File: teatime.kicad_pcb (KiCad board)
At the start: 2 copper layers, 100 x 100 mm, 64 parts, among them Q1 NCV8402, Q2 NCV8402, Q3 NCV8402, Q4 NCV8402, Q5 NCV8402, Q6 NCV8402, Q7 NCV8402, Q8 NCV8402, SW1 SW_Push, U1 NCP1117-3.3_SOT223, U2 74HC4051

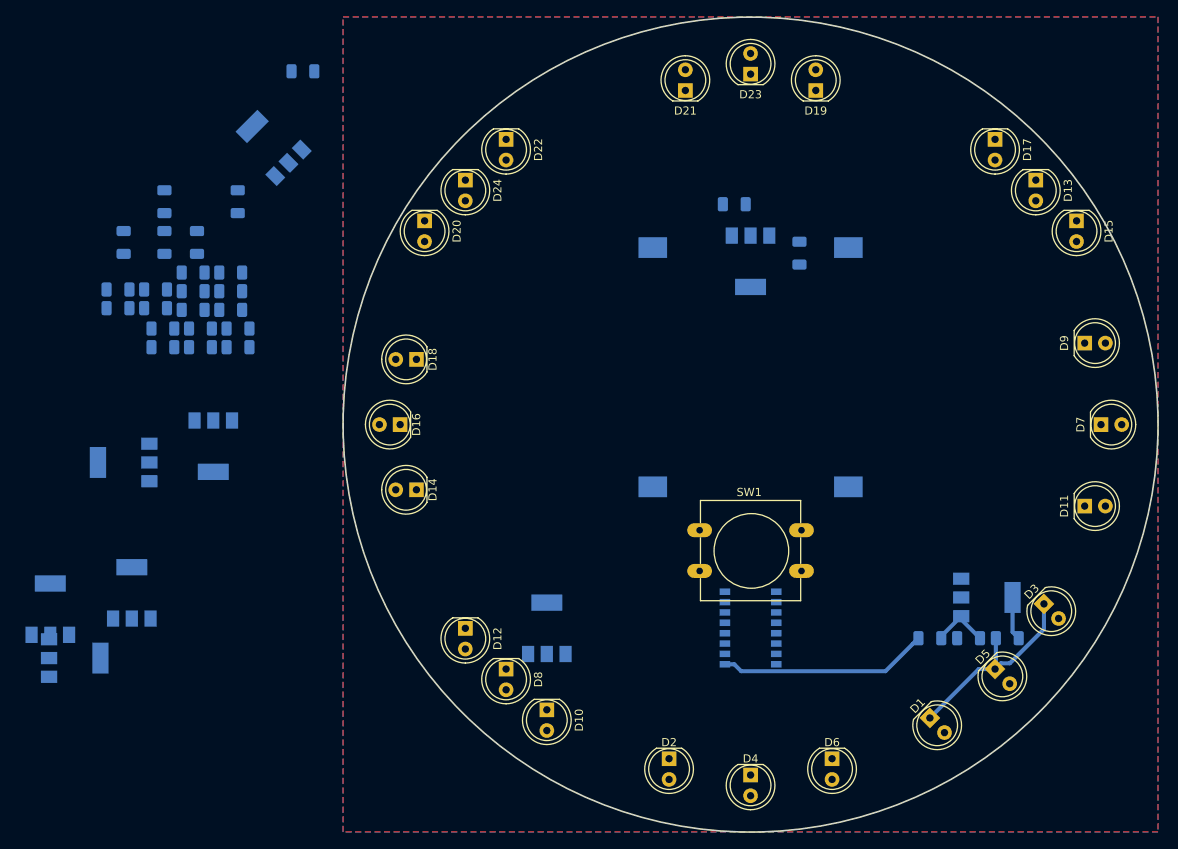
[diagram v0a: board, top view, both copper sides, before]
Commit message: Shift regs and led layout
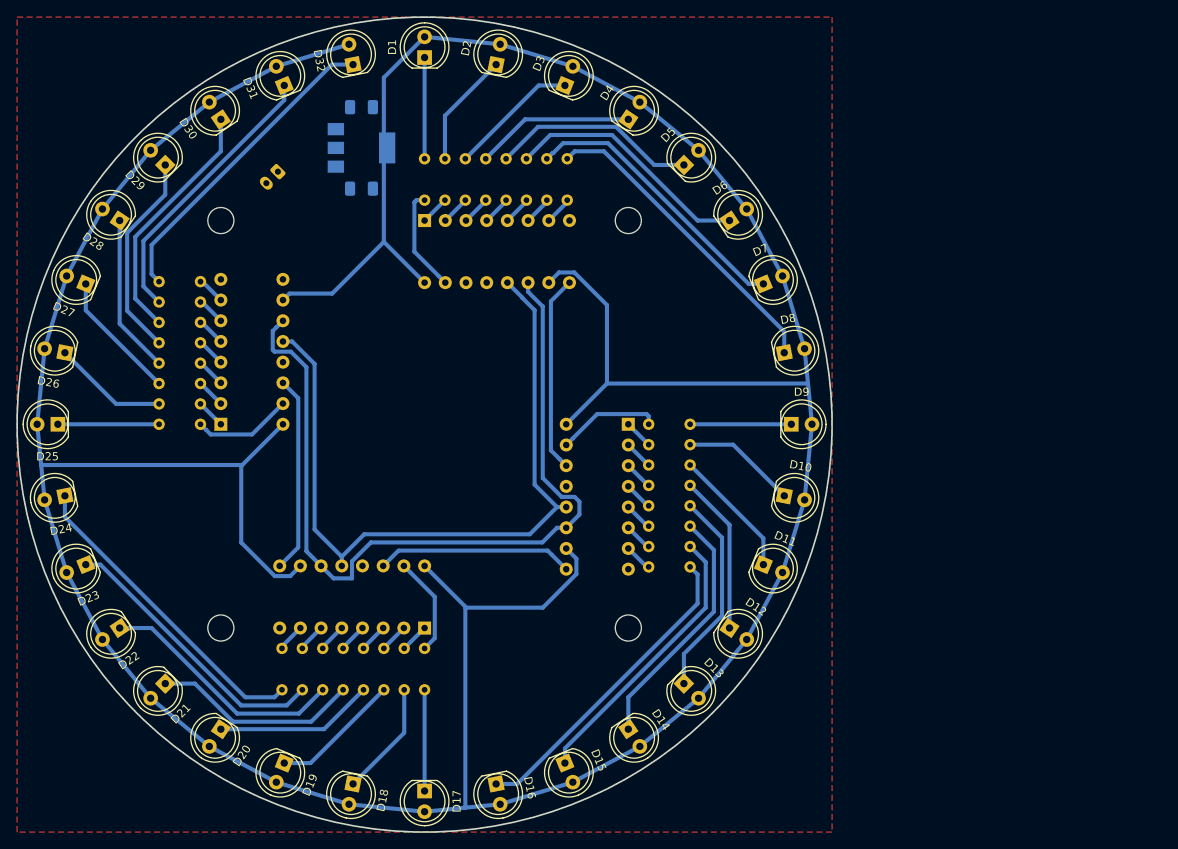
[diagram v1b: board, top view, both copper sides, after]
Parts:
- removed BT2: Battery_Cell, Battery:BatteryHolder_Keystone_1058_1x2032
- removed Q1, Q2, Q3, Q4, Q5, Q6, Q7, Q8: NCV8402, Package_TO_SOT_SMD:SOT-223-3_TabPin2
- removed SW1: SW_Push, Button_Switch_THT:SW_PUSH-12mm
- added D25: LED, LED_THT:LED_D5.0mm, F.Cu at (55.0, 100.0)
- added D26: LED, LED_THT:LED_D5.0mm, F.Cu at (55.9, 91.2)
- added D27: LED, LED_THT:LED_D5.0mm, F.Cu at (58.4, 82.8)
- added D28: LED, LED_THT:LED_D5.0mm, F.Cu at (62.6, 75.0)
- added D29: LED, LED_THT:LED_D5.0mm, F.Cu at (68.2, 68.2)
- added D30: LED, LED_THT:LED_D5.0mm, F.Cu at (75.0, 62.6)
- added D31: LED, LED_THT:LED_D5.0mm, F.Cu at (82.8, 58.4)
- added D32: LED, LED_THT:LED_D5.0mm, F.Cu at (91.2, 55.9)
- added H1: MountingHole, MountingHole:MountingHole_3.2mm_M3, F.Cu at (75.0, 75.0)
- added H2: MountingHole, MountingHole:MountingHole_3.2mm_M3, F.Cu at (125.0, 75.0)
- added H3: MountingHole, MountingHole:MountingHole_3.2mm_M3, F.Cu at (125.0, 125.0)
- added H4: MountingHole, MountingHole:MountingHole_3.2mm_M3, F.Cu at (75.0, 125.0)
- added R26: 680r, Resistor_THT:R_Axial_DIN0204_L3.6mm_D1.6mm_P5.08mm_Horizontal, B.Cu at (72.5, 97.5)
- added R27: 680r, Resistor_THT:R_Axial_DIN0204_L3.6mm_D1.6mm_P5.08mm_Horizontal, B.Cu at (72.5, 95.0)
- added R28: 680r, Resistor_THT:R_Axial_DIN0204_L3.6mm_D1.6mm_P5.08mm_Horizontal, B.Cu at (72.5, 92.5)
- added R29: 680r, Resistor_THT:R_Axial_DIN0204_L3.6mm_D1.6mm_P5.08mm_Horizontal, B.Cu at (72.5, 90.0)
- added R30: 680r, Resistor_THT:R_Axial_DIN0204_L3.6mm_D1.6mm_P5.08mm_Horizontal, B.Cu at (72.5, 87.5)
- added R31: 680r, Resistor_THT:R_Axial_DIN0204_L3.6mm_D1.6mm_P5.08mm_Horizontal, B.Cu at (72.5, 85.0)
- added R32: 680r, Resistor_THT:R_Axial_DIN0204_L3.6mm_D1.6mm_P5.08mm_Horizontal, B.Cu at (72.5, 82.5)
- added U3: 74HC596, Package_DIP:DIP-16_W7.62mm, B.Cu at (125.0, 100.0)
- added U4: 74HC596, Package_DIP:DIP-16_W7.62mm, B.Cu at (100.0, 125.0)
- added U5: 74HC596, Package_DIP:DIP-16_W7.62mm, B.Cu at (75.0, 100.0)
- BT1: footprint Battery:BatteryHolder_Keystone_1058_1x2032 -> Connector_JST:JST_PH_S2B-PH-K_1x02_P2.00mm_Horizontal
- D1, D10, D11, D12, D13, D14, D15, D16, D17, D18, D19, D2, D20, D21, D22, D23, D24, D3, D4, D5, D6, D7, D8, D9: footprint LED_THT:LED_D5.0mm_Clear -> LED_THT:LED_D5.0mm
- R1, R12, R13, R18, R19, R2, R24, R25, R7: value R_Small -> 680r; footprint Resistor_SMD:R_1206_3216Metric -> Resistor_THT:R_Axial_DIN0204_L3.6mm_D1.6mm_P5.08mm_Horizontal
- R10, R11, R16, R17, R22, R23, R5, R6: value 100k -> 680r; footprint Resistor_SMD:R_1206_3216Metric -> Resistor_THT:R_Axial_DIN0204_L3.6mm_D1.6mm_P5.08mm_Horizontal
- R14, R15, R20, R21, R3, R4, R8, R9: value 1k -> 680r; footprint Resistor_SMD:R_1206_3216Metric -> Resistor_THT:R_Axial_DIN0204_L3.6mm_D1.6mm_P5.08mm_Horizontal
- U2: value 74HC4051 -> 74HC596; footprint Package_SO:SOP-16_4.4x10.4mm_P1.27mm -> Package_DIP:DIP-16_W7.62mm
- moved D17 106.3 mm to (100.0, 145.0)
- moved D19 105.2 mm to (82.8, 141.6), turned to 247.5 degrees
- moved D1 102.0 mm to (100.0, 55.0), turned to 90 degrees
- moved D23 101.4 mm to (58.4, 117.2), turned to 202.5 degrees
- moved D21 96.8 mm to (68.2, 131.8), turned to 225 degrees
- moved D15 91.5 mm to (117.2, 141.6), turned to 292.5 degrees
- moved D2 87.8 mm to (108.8, 55.9), turned to 78.75 degrees
- moved R2 87.5 mm to (102.5, 72.5), turned to 90 degrees
- moved D3 86.6 mm to (117.2, 58.4), turned to 67.5 degrees
- moved D4 81.8 mm to (125.0, 62.6), turned to 56.25 degrees
- moved R3 78.3 mm to (105.0, 72.5), turned to 90 degrees
- moved R5 78.2 mm to (110.0, 72.5), turned to 90 degrees
- moved D22 76.4 mm to (62.6, 125.0), turned to 213.75 degrees
- moved D13 75.4 mm to (131.8, 131.8), turned to 315 degrees
- moved BT1 74.0 mm to (82.0, 69.0), turned to 225 degrees
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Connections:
- BT1 pad 2: Net-(BT1-Pad2) -> GND
- C2 pad 1: VCC -> +3V3
- D1 pad 2: VCC -> +3V3
- D10 pad 2: VCC -> +3V3
- D11 pad 2: VCC -> +3V3
- D12 pad 1: Net-(D10-Pad1) -> Net-(D12-Pad1)
- D12 pad 2: VCC -> +3V3
- D13 pad 2: VCC -> +3V3
- D14 pad 2: VCC -> +3V3
- D15 pad 1: Net-(D13-Pad1) -> Net-(D15-Pad1)
- D15 pad 2: VCC -> +3V3
- D16 pad 1: Net-(D14-Pad1) -> Net-(D16-Pad1)
- D16 pad 2: VCC -> +3V3
- D17 pad 1: Net-(D13-Pad1) -> Net-(D17-Pad1)
- D17 pad 2: VCC -> +3V3
- D18 pad 1: Net-(D14-Pad1) -> Net-(D18-Pad1)
- D18 pad 2: VCC -> +3V3
- D19 pad 2: VCC -> +3V3
- D2 pad 2: VCC -> +3V3
- D20 pad 2: VCC -> +3V3
- D21 pad 1: Net-(D19-Pad1) -> Net-(D21-Pad1)
- D21 pad 2: VCC -> +3V3
- D22 pad 1: Net-(D20-Pad1) -> Net-(D22-Pad1)
- D22 pad 2: VCC -> +3V3
- D23 pad 1: Net-(D19-Pad1) -> Net-(D23-Pad1)
- D23 pad 2: VCC -> +3V3
- D24 pad 1: Net-(D20-Pad1) -> Net-(D24-Pad1)
- D24 pad 2: VCC -> +3V3
- D3 pad 1: Net-(D1-Pad1) -> Net-(D3-Pad1)
- D3 pad 2: VCC -> +3V3
- D4 pad 1: Net-(D2-Pad1) -> Net-(D4-Pad1)
- D4 pad 2: VCC -> +3V3
- D5 pad 1: Net-(D1-Pad1) -> Net-(D5-Pad1)
- D5 pad 2: VCC -> +3V3
- D6 pad 1: Net-(D2-Pad1) -> Net-(D6-Pad1)
- D6 pad 2: VCC -> +3V3
- D7 pad 1: Net-(D11-Pad1) -> Net-(D7-Pad1)
- D7 pad 2: VCC -> +3V3
- D8 pad 1: Net-(D10-Pad1) -> Net-(D8-Pad1)
- D8 pad 2: VCC -> +3V3
- D9 pad 1: Net-(D11-Pad1) -> Net-(D9-Pad1)
- D9 pad 2: VCC -> +3V3
- R1 pad 2: GND -> Net-(D1-Pad1)
- R10 pad 1: Net-(Q3-Pad1) -> Net-(R10-Pad1)
- R10 pad 2: GND -> Net-(D10-Pad1)
- R11 pad 1: Net-(Q4-Pad1) -> Net-(R11-Pad1)
- R11 pad 2: GND -> Net-(D11-Pad1)
- R12 pad 1: Net-(D11-Pad1) -> Net-(R12-Pad1)
- R12 pad 2: Net-(Q3-Pad2) -> Net-(D12-Pad1)
- R13 pad 1: Net-(D10-Pad1) -> Net-(R13-Pad1)
- R13 pad 2: Net-(Q4-Pad2) -> Net-(D13-Pad1)
- R14 pad 1: Net-(Q5-Pad1) -> Net-(R14-Pad1)
- R14 pad 2: Net-(R14-Pad2) -> Net-(D14-Pad1)
- R15 pad 1: Net-(Q6-Pad1) -> Net-(R15-Pad1)
- R15 pad 2: Net-(R15-Pad2) -> Net-(D15-Pad1)
- R16 pad 1: Net-(Q5-Pad1) -> Net-(R16-Pad1)
- R16 pad 2: GND -> Net-(D16-Pad1)
- R17 pad 1: Net-(Q6-Pad1) -> Net-(R17-Pad1)
- R17 pad 2: GND -> Net-(D17-Pad1)
- R18 pad 1: Net-(D13-Pad1) -> Net-(R18-Pad1)
- R18 pad 2: Net-(Q5-Pad2) -> Net-(D18-Pad1)
- R19 pad 1: Net-(D14-Pad1) -> Net-(R19-Pad1)
- R19 pad 2: Net-(Q6-Pad2) -> Net-(D19-Pad1)
- R2 pad 1: Net-(D1-Pad1) -> Net-(R2-Pad1)
- R2 pad 2: Net-(Q1-Pad2) -> Net-(D2-Pad1)
- R20 pad 1: Net-(Q7-Pad1) -> Net-(R20-Pad1)
- R20 pad 2: Net-(R20-Pad2) -> Net-(D20-Pad1)
- R21 pad 1: Net-(Q8-Pad1) -> Net-(R21-Pad1)
- R21 pad 2: Net-(R21-Pad2) -> Net-(D21-Pad1)
- R22 pad 1: Net-(Q7-Pad1) -> Net-(R22-Pad1)
- R22 pad 2: GND -> Net-(D22-Pad1)
- R23 pad 1: Net-(Q8-Pad1) -> Net-(R23-Pad1)
- R23 pad 2: GND -> Net-(D23-Pad1)
- R24 pad 1: Net-(D19-Pad1) -> Net-(R24-Pad1)
- R24 pad 2: Net-(Q7-Pad2) -> Net-(D24-Pad1)
- R25 pad 1: Net-(D20-Pad1) -> Net-(R25-Pad1)
- R3 pad 1: Net-(Q1-Pad1) -> Net-(R3-Pad1)
- R3 pad 2: Net-(R3-Pad2) -> Net-(D3-Pad1)
- R4 pad 1: Net-(Q2-Pad1) -> Net-(R4-Pad1)
- R4 pad 2: Net-(R4-Pad2) -> Net-(D4-Pad1)
- R5 pad 1: Net-(Q1-Pad1) -> Net-(R5-Pad1)
- R5 pad 2: GND -> Net-(D5-Pad1)
- R6 pad 1: Net-(Q2-Pad1) -> Net-(R6-Pad1)
- R6 pad 2: GND -> Net-(D6-Pad1)
- R7 pad 1: Net-(D2-Pad1) -> Net-(R7-Pad1)
- R7 pad 2: Net-(Q2-Pad2) -> Net-(D7-Pad1)
- R8 pad 1: Net-(Q3-Pad1) -> Net-(R8-Pad1)
- R8 pad 2: Net-(R8-Pad2) -> Net-(D8-Pad1)
- R9 pad 1: Net-(Q4-Pad1) -> Net-(R9-Pad1)
- R9 pad 2: Net-(R9-Pad2) -> Net-(D9-Pad1)
- U1 pad 2: VCC -> +3V3
- U2 pad 1: Net-(R3-Pad2) -> Net-(R2-Pad1)
- U2 pad 10: Net-(U2-Pad10) -> +3V3
- U2 pad 12: Net-(R21-Pad2) -> Net-(U2-Pad12)
- U2 pad 13: Net-(R14-Pad2) -> GND
- U2 pad 14: Net-(R20-Pad2) -> Net-(U2-Pad14)
- U2 pad 15: Net-(R15-Pad2) -> Net-(R1-Pad1)
- U2 pad 16: VCC -> +3V3
- U2 pad 2: Net-(R4-Pad2) -> Net-(R3-Pad1)
- U2 pad 3: Net-(U2-Pad3) -> Net-(R4-Pad1)
- U2 pad 4: Net-(R9-Pad2) -> Net-(R5-Pad1)
- U2 pad 5: Net-(R8-Pad2) -> Net-(R6-Pad1)
- U2 pad 6: GND -> Net-(R7-Pad1)
- U2 pad 7: GND -> Net-(R8-Pad1)
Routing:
- net +3V3: track 0.00 -> 490.7 mm
- net Net-(U2-Pad11): track 0.00 -> 103.0 mm
- net Net-(U2-Pad12): track 0.00 -> 91.3 mm
- net Net-(D24-Pad1): track 0.00 -> 38.8 mm
- net Net-(D16-Pad1): track 0.00 -> 38.8 mm
- net Net-(D32-Pad1): track 0.00 -> 38.8 mm
- net Net-(D8-Pad1): track 0.00 -> 38.8 mm
- net Net-(D23-Pad1): track 0.00 -> 34.5 mm
- net Net-(D31-Pad1): track 0.00 -> 34.5 mm
- net Net-(D15-Pad1): track 0.00 -> 34.5 mm
- net Net-(D7-Pad1): track 0.00 -> 34.5 mm
- net Net-(D22-Pad1): track 0.00 -> 30.5 mm
- net Net-(D30-Pad1): track 0.00 -> 30.5 mm
- net Net-(D14-Pad1): track 0.00 -> 30.5 mm
- net Net-(D6-Pad1): track 0.00 -> 30.5 mm
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- added copper zone on F.Cu, net GND
- removed copper zone on B.Cu, net GND
- removed copper zone on F.Cu, net VCC
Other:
- net class Default: trace_width 0.25 -> 0.5; via_dia 0.8 -> 0.6; via_drill 0.4 -> 0.3

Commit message: Add micro and tweak some other bits
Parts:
- added R33: 100k, Resistor_THT:R_Axial_DIN0204_L3.6mm_D1.6mm_P5.08mm_Horizontal, F.Cu at (107.5, 97.5)
- added SW1: SW_Push, Button_Switch_THT:SW_PUSH_6mm, F.Cu at (97.5, 97.5)
- added U6: ATtiny85-20PU, Package_DIP:DIP-8_W7.62mm, F.Cu at (97.5, 95.0)
- R1, R10, R11, R12, R13, R14, R15, R16, R17, R18, R19, R2, R20, R21, R22, R23, R24, R25, R26, R27, R28, R29, R3, R30, R31, R32, R4, R5, R6, R7, R8, R9: value 680r -> 220r; moved to F.Cu
- U1: value NCP1117-3.3_SOT223 -> MCP1700-3302E_TO92; footprint Package_TO_SOT_SMD:SOT-223-3_TabPin2 -> Package_TO_SOT_THT:TO-92_Inline; moved to F.Cu
- U2, U3, U4, U5: moved to F.Cu
- moved R32 113.0 mm to (184.6, 97.0), turned to 0 degrees
- moved R25 112.5 mm to (184.6, 90.7), turned to 0 degrees
- moved R31 112.5 mm to (184.6, 93.8), turned to 0 degrees
- moved R30 105.3 mm to (176.6, 103.2), turned to 0 degrees
- moved R22 105.0 mm to (184.6, 87.5), turned to 0 degrees
- moved R29 104.6 mm to (176.6, 100.1), turned to 0 degrees
- moved R26 104.1 mm to (176.6, 97.0), turned to 0 degrees
- moved R24 99.9 mm to (176.6, 93.8), turned to 0 degrees
- moved R28 97.1 mm to (168.6, 106.4), turned to 0 degrees
- moved R27 96.4 mm to (168.6, 103.2), turned to 0 degrees
- moved R23 87.9 mm to (168.6, 100.1), turned to 0 degrees
- moved R18 87.3 mm to (176.6, 90.7), turned to 0 degrees
- moved R19 79.7 mm to (168.6, 97.0), turned to 0 degrees
- moved R17 76.4 mm to (168.6, 93.8), turned to 0 degrees
- moved R21 73.6 mm to (160.5, 106.4), turned to 0 degrees
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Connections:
- U1 pad 2: +3V3 -> Net-(BT1-Pad1)
- U1 pad 3: Net-(BT1-Pad1) -> +3V3
- U5 pad 9: Net-(U5-Pad9) -> (no net)
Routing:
- net +3V3: track 490.7 -> 0.00 mm
- net Net-(U2-Pad11): track 103.0 -> 0.00 mm
- net Net-(U2-Pad12): track 91.3 -> 0.00 mm
- net Net-(D24-Pad1): track 38.8 -> 0.00 mm
- net Net-(D16-Pad1): track 38.8 -> 0.00 mm
- net Net-(D32-Pad1): track 38.8 -> 0.00 mm
- net Net-(D8-Pad1): track 38.8 -> 0.00 mm
- net Net-(D23-Pad1): track 34.5 -> 0.00 mm
- net Net-(D31-Pad1): track 34.5 -> 0.00 mm
- net Net-(D15-Pad1): track 34.5 -> 0.00 mm
- net Net-(D7-Pad1): track 34.5 -> 0.00 mm
- net Net-(D22-Pad1): track 30.5 -> 0.00 mm
- net Net-(D30-Pad1): track 30.5 -> 0.00 mm
- net Net-(D14-Pad1): track 30.5 -> 0.00 mm
- net Net-(D6-Pad1): track 30.5 -> 0.00 mm
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
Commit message: More tweaks and v1 version of board
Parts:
- added C3: 100n, Capacitor_THT:C_Disc_D3.0mm_W1.6mm_P2.50mm, F.Cu at (106.5, 90.0)
- C1, C2: value 10u -> 1u; moved to F.Cu
- moved R15 107.7 mm to (72.5, 115.0), turned to 180 degrees
- moved R11 97.1 mm to (72.5, 105.0), turned to 180 degrees
- moved D25 90.0 mm to (145.0, 100.0), turned to 0 degrees
- moved D9 90.0 mm to (55.0, 100.0), turned to 180 degrees
- moved R16 89.7 mm to (72.5, 117.5), turned to 180 degrees
- moved R12 88.7 mm to (72.5, 107.5), turned to 180 degrees
- moved R10 88.5 mm to (72.5, 102.5), turned to 180 degrees
- moved D10 88.3 mm to (55.9, 108.8), turned to 191.25 degrees
- moved D24 88.3 mm to (144.1, 108.8), turned to 348.75 degrees
- moved D26 88.3 mm to (144.1, 91.2), turned to 11.25 degrees
- moved D8 88.3 mm to (55.9, 91.2), turned to 168.75 degrees
- moved R8 87.4 mm to (82.5, 72.5), turned to 90 degrees
- moved D11 83.1 mm to (58.4, 117.2), turned to 202.5 degrees
- moved D23 83.1 mm to (141.6, 117.2), turned to 337.5 degrees
- moved D27 83.1 mm to (141.6, 82.8), turned to 22.5 degrees
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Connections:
- U5 pad 9: (no net) -> Net-(U5-Pad9)
- U6 pad 2: (no net) -> Net-(U6-Pad2)
- U6 pad 3: (no net) -> Net-(U6-Pad3)
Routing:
- net +3V3: track 0.00 -> 517.4 mm
- net Net-(U2-Pad11): track 0.00 -> 120.1 mm
- net Net-(U2-Pad12): track 0.00 -> 102.2 mm
- net Net-(D8-Pad1): track 0.00 -> 38.8 mm
- net Net-(D32-Pad1): track 0.00 -> 38.8 mm
- net Net-(D16-Pad1): track 0.00 -> 38.8 mm
- net Net-(D24-Pad1): track 0.00 -> 38.8 mm
- net Net-(D7-Pad1): track 0.00 -> 34.5 mm
- net Net-(D15-Pad1): track 0.00 -> 34.5 mm
- net Net-(D31-Pad1): track 0.00 -> 34.5 mm
- net Net-(D23-Pad1): track 0.00 -> 34.5 mm
- net Net-(D14-Pad1): track 0.00 -> 30.5 mm
- net Net-(D6-Pad1): track 0.00 -> 30.5 mm
- net Net-(D22-Pad1): track 0.00 -> 30.5 mm
- net Net-(D30-Pad1): track 0.00 -> 30.5 mm
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- added copper zone on B.Cu, net GND
- removed copper zone on F.Cu, net GND
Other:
- net class vcc added: clearance 0.2, trace_width 1, via_dia 0.6, via_drill 0.3

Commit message: Few slight tweaks to footprints used and updated build files
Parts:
- C3: footprint Capacitor_THT:C_Disc_D3.0mm_W1.6mm_P2.50mm -> Capacitor_SMD:C_1206_3216Metric
- U1: footprint Package_TO_SOT_THT:TO-92_Inline -> Package_TO_SOT_THT:TO-92_Inline_W4.0mm_Horizontal_FlatSideDown
- U2, U3, U4, U5: value 74HC596 -> 74HC595
- moved C3 1.25 mm to (106.5, 91.2)
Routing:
- net GND: track 13.5 -> 17.8 mm

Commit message: Few small tweaks and add silk
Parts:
- added C4: 100n, Capacitor_SMD:C_1206_3216Metric, F.Cu at (103.8, 81.2)
- added C5: 100n, Capacitor_SMD:C_1206_3216Metric, F.Cu at (81.0, 96.2)
- added C6: 100n, Capacitor_SMD:C_1206_3216Metric, F.Cu at (96.2, 119.0)
- added C7: 100n, Capacitor_SMD:C_1206_3216Metric, F.Cu at (119.0, 103.8)
- added HS1: QR, teatime:__github.com_HarkonenBade_teatime, B.Cu at (70.0, 87.5)
- R1, R10, R11, R12, R13, R14, R15, R16, R17, R18, R19, R2, R20, R21, R22, R23, R24, R25, R26, R27, R28, R29, R3, R30, R31, R32, R33, R4, R5, R6, R7, R8, R9: footprint Resistor_THT:R_Axial_DIN0204_L3.6mm_D1.6mm_P5.08mm_Horizontal -> Resistor_THT:R_Axial_DIN0204_L3.6mm_D1.6mm_P7.62mm_Horizontal
- U1: value MCP1700-3302E_TO92 -> MCP1700-3302E
- moved R33 2.12 mm to (93.0, 95.0)
- moved R16 0.28 mm to (72.5, 117.8)
- moved R24 0.28 mm to (117.8, 127.5)
- moved R32 0.28 mm to (127.5, 82.2)
- moved R8 0.28 mm to (82.2, 72.5)
- moved R15 0.24 mm to (72.5, 115.2)
- moved R23 0.24 mm to (115.2, 127.5)
- moved R31 0.24 mm to (127.5, 84.8)
- moved R7 0.24 mm to (84.8, 72.5)
- moved R14 0.20 mm to (72.5, 112.7)
- moved R22 0.20 mm to (112.7, 127.5)
- moved R30 0.20 mm to (127.5, 87.3)
- moved R6 0.20 mm to (87.3, 72.5)
- moved R13 0.16 mm to (72.5, 110.2)
- moved R21 0.16 mm to (110.2, 127.5)
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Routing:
- net GND: track 17.8 -> 22.2 mm, vias 0 -> 4
- net Net-(D2-Pad1): track 14.2 -> 11.6 mm
- net Net-(D10-Pad1): track 14.2 -> 11.6 mm
- net Net-(D26-Pad1): track 14.2 -> 11.6 mm
- net Net-(D18-Pad1): track 14.2 -> 11.6 mm
- net Net-(D9-Pad1): track 12.4 -> 9.88 mm
- net Net-(D1-Pad1): track 12.4 -> 9.88 mm
- net Net-(D25-Pad1): track 12.4 -> 9.88 mm
- net Net-(D17-Pad1): track 12.4 -> 9.88 mm
- net Net-(R33-Pad1): track 14.7 -> 12.6 mm
- net +3V3: track 517.4 -> 515.4 mm
- net Net-(D20-Pad1): track 19.5 -> 20.1 mm
- net Net-(D4-Pad1): track 19.5 -> 20.1 mm
- net Net-(D28-Pad1): track 19.5 -> 20.1 mm
- net Net-(D12-Pad1): track 19.5 -> 20.1 mm
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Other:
- board text added: "+"
- board text added: "-"
- board text added: "Lithium Primary 3.5V Min"
- board text added: "Teatime HarkonenBade 2020-02-14 Rev 1"
- board text added: "https://github.com/HarkonenBade/teatime"

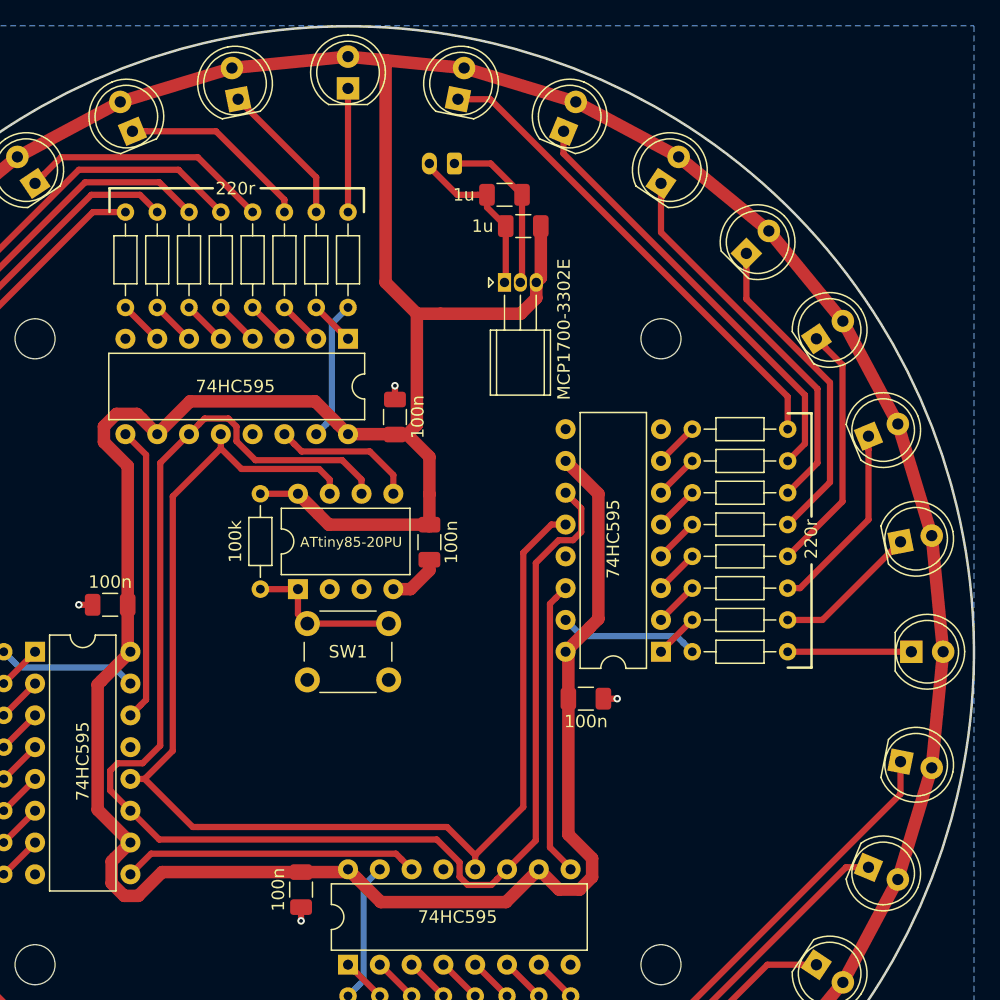
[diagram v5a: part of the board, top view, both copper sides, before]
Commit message: Switch around various bits: * Add decoupling * Omron button * pth caps
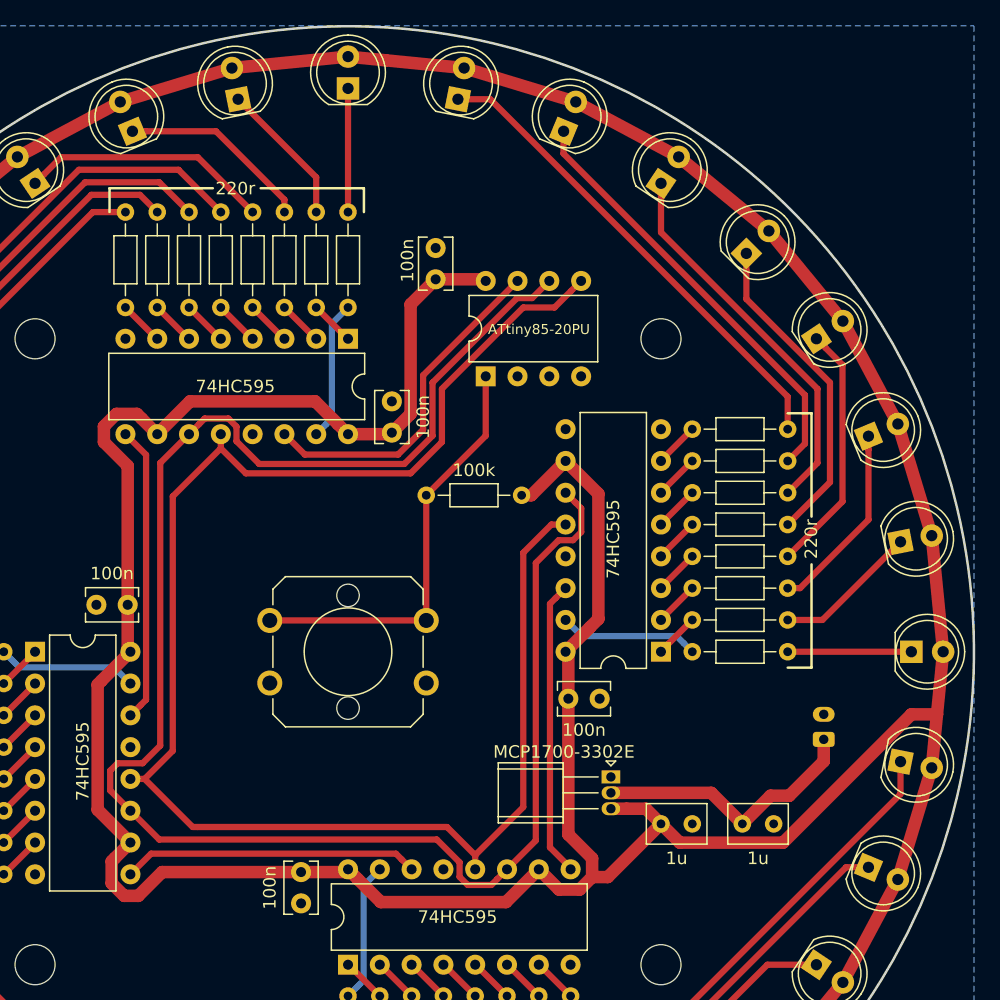
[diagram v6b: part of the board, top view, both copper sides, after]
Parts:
- C1, C2: footprint Capacitor_SMD:C_1206_3216Metric -> Capacitor_THT:C_Rect_L4.6mm_W3.0mm_P2.50mm_MKS02_FKP02
- C3, C4, C5, C6, C7: footprint Capacitor_SMD:C_1206_3216Metric -> Capacitor_THT:C_Rect_L4.0mm_W2.5mm_P2.50mm
- SW1: footprint Button_Switch_THT:SW_PUSH_6mm -> teatime:B3F-40xx
- moved BT1 54.6 mm to (138.0, 107.0), turned to 90 degrees
- moved C1 53.7 mm to (131.5, 113.8), turned to 0 degrees
- moved C2 49.0 mm to (125.0, 113.8), turned to 0 degrees
- moved U1 40.4 mm to (121.0, 110.0), turned to 270 degrees
- moved U6 22.7 mm to (111.0, 78.0)
- moved C3 21.0 mm to (107.0, 70.2), turned to 90 degrees
- moved R33 15.2 mm to (106.2, 87.5), turned to 0 degrees
- moved SW1 3.95 mm to (100.0, 100.0), turned to 180 degrees
- moved C5 1.40 mm to (82.4, 96.2)
- moved C6 1.40 mm to (96.2, 117.6)
- moved C7 1.40 mm to (117.6, 103.8)
- moved C4 1.27 mm to (103.5, 82.5)
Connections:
- U6 pad 5: Net-(U2-Pad14) -> Net-(U2-Pad12)
- U6 pad 7: Net-(U2-Pad12) -> Net-(U2-Pad14)
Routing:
- net Net-(U2-Pad12): track 102.2 -> 129.8 mm
- net GND: track 22.2 -> 0.00 mm, vias 4 -> 0
- net Net-(U2-Pad11): track 120.1 -> 142.0 mm
- net Net-(R33-Pad1): track 12.6 -> 34.0 mm
- net Net-(U2-Pad14): track 11.6 -> 27.6 mm
- net +3V3: track 515.4 -> 505.2 mm
- net Net-(BT1-Pad1): track 13.6 -> 21.8 mm
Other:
- board text added: "github.com/HarkonenBade/teatime"
- board text removed: "https://github.com/HarkonenBade/teatime"
